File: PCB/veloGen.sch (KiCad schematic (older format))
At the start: 25 parts, among them J1 Conn_01x06, J2 Gen. IN, J3 Bat, J4 Conn_01x04, U1 ESP-WROOM-32, U2 TS1101-100EG6T, U4 MAX8881

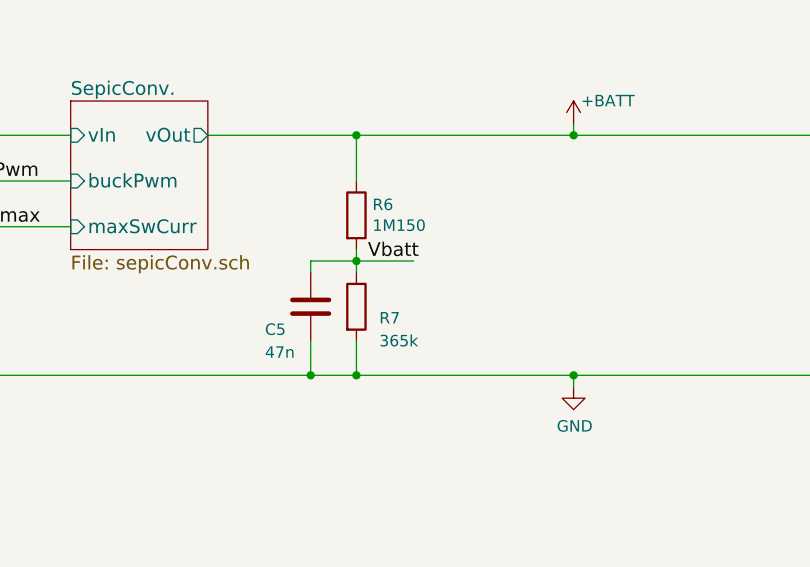
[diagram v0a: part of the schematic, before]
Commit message: Fixed the linear calibration factor for VBatt
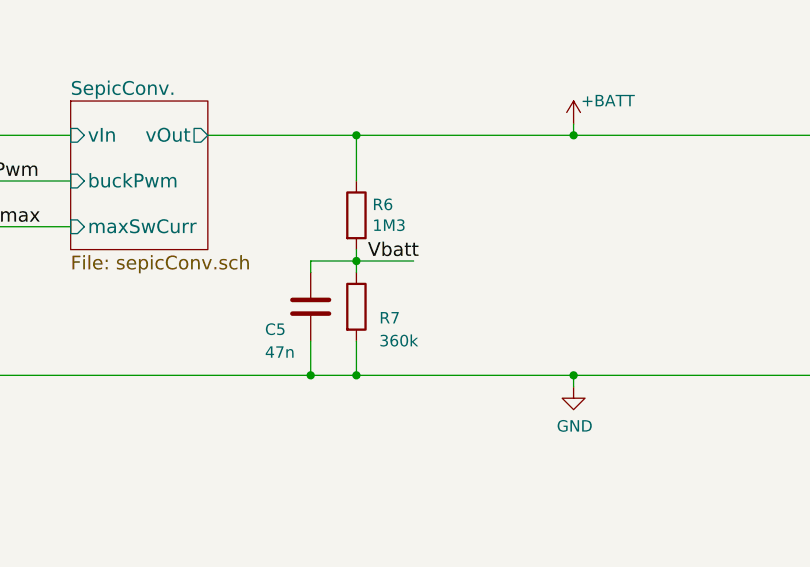
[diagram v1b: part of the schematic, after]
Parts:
- R6: value 1M150 -> 1M3
- R7: value 365k -> 360k
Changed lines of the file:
@@
 LIBS:power
 LIBS:device
-LIBS:transistors
-LIBS:conn
 LIBS:linear
 LIBS:regul
-LIBS:74xx
-LIBS:cmos4000
 LIBS:adc-dac
 LIBS:memory
@@
 LIBS:digital-audio
 LIBS:philips
-LIBS:display
 LIBS:cypress
 LIBS:siliconi
@@
 LIBS:atmel
 LIBS:contrib
-LIBS:valves
 LIBS:veloGen-cache
 EELAYER 26 0
@@
 P 6050 2850
 F 0 "R6" H 6120 2896 50  0000 L CNN
-F 1 "1M150" H 6120 2805 50  0000 L CNN
+F 1 "1M3" H 6120 2805 50  0000 L CNN
 F 2 "Resistors_SMD:R_0805" V 5980 2850 50  0001 C CNN
 F 3 "" H 6050 2850 50  0001 C CNN
@@
 P 6050 3250
 F 0 "R7" H 6150 3200 50  0000 L CNN
-F 1 "365k" H 6150 3100 50  0000 L CNN
+F 1 "360k" H 6150 3100 50  0000 L CNN
 F 2 "Resistors_SMD:R_0805" V 5980 3250 50  0001 C CNN
 F 3 "" H 6050 3250 50  0001 C CNN

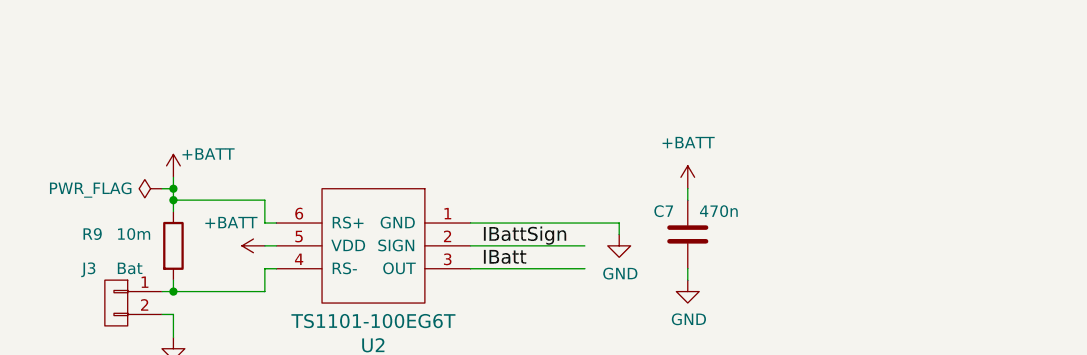
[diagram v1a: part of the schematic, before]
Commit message: Added I-sense cal constants
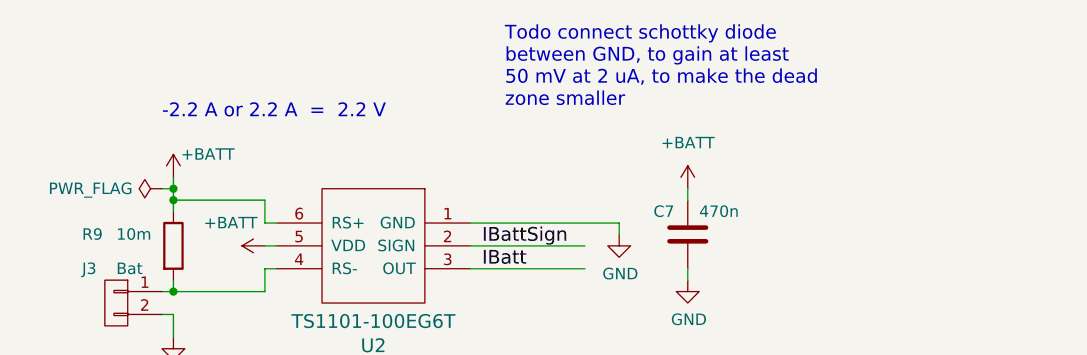
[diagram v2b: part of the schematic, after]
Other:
- note added: "-2.2 A or 2.2 A = 2.2 V"
- note added: "Todo connect schottky diode\nbetween GND, to gain at least\n50 mV at 2 uA, to make the dead\nzone smaller"
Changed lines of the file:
@@
 Text Notes 750  2450 0    60   ~ 0
 MOsfet mirrored\nProg con mirrored\n3.3 reg to wimpy
+Text Notes 1550 1000 0    60   ~ 0
+-2.2 A or 2.2 A  =  2.2 V
+Text Notes 3050 950  0    60   ~ 0
+Todo connect schottky diode\nbetween GND, to gain at least\n50 mV at 2 uA, to make the dead\nzone smaller
 $EndSCHEMATC

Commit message: stuff
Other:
- note added: "Moved speedPulse to IO2 to allow for wakeup"
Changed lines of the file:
@@
 Text Notes 3050 950  0    60   ~ 0
 Todo connect schottky diode\nbetween GND, to gain at least\n50 mV at 2 uA, to make the dead\nzone smaller
+Text Notes 4400 6950 0    60   ~ 0
+Moved speedPulse to IO2 to allow for wakeup
 $EndSCHEMATC
